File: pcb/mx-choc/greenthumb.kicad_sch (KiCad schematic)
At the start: 63 parts, among them J1 Conn_01x02_Female, M1 XIAO-RP2040, SW11 SW_Push, SW12 SW_Push, SW13 SW_Push, SW14 SW_Push, SW15 SW_Push, SW16 SW_Push, SW17 SW_Push, SW18 SW_Push, SW19 SW_Push, SW2 SW_Push, SW20 SW_Push, SW21 SW_Push, SW22 SW_Push, SW23 SW_Push, SW24 SW_Push, SW25 SW_Push, SW26 SW_Push, SW27 SW_Push, SW28 SW_Push, SW29 SW_Push, SW3 SW_Push, SW30 SW_Push, SW33 SW_Push, SW34 SW_Push, SW35 SW_Push, SW36 SW_Push, SW37 SW_Push, SW38 SW_Push, SW41 SW_Push, SW8 SW_Push, SW9 SW_Push

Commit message: routing almost done
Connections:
- net col0: now also SW35.2, SW36.2
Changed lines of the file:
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@@
   (junction (at 150.495 114.935) (diameter 0) (color 0 0 0 0)
+  )
+  (junction (at 133.985 114.935) (diameter 0) (color 0 0 0 0)
   )
   (junction (at 200.025 114.935) (diameter 0) (color 0 0 0 0)
@@
   )
   (junction (at 183.515 61.595) (diameter 0) (color 0 0 0 0)
+  )
+  (junction (at 133.985 88.265) (diameter 0) (color 0 0 0 0)
   )
   (junction (at 173.355 42.545) (diameter 0) (color 0 0 0 0)
@@
   )
   (wire (pts (xy 216.535 34.925) (xy 216.535 61.595))
+    (stroke (width 0) (type default) (color 0 0 0 0))
+  )
+  (wire (pts (xy 133.985 114.935) (xy 133.985 141.605))
     (stroke (width 0) (type default) (color 0 0 0 0))
   )
@@
     (stroke (width 0) (type default) (color 0 0 0 0))
   )
+  (wire (pts (xy 133.985 88.265) (xy 133.985 114.935))
+    (stroke (width 0) (type default) (color 0 0 0 0))
+  )

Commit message: completed pcb
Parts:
- added H1: MountingHole, fingerpunch:fingerpunch-logo, symbol Mechanical:MountingHole
- M1: LCSC (none) -> 102010428; Seeed SKU (none) -> 102010428
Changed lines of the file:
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@@
+      (effects (font (size 1.27 1.27)) hide)
+    )
+    (property "Seeed SKU" "" (id 5) (at 140.335 38.735 90)
       (effects (font (size 1.27 1.27)) hide)
     )
@@
       (effects (font (size 1.27 1.27)) hide)
     )
+    (property "Seeed SKU" "" (id 5) (at 156.845 38.735 90)
+      (effects (font (size 1.27 1.27)) hide)
+    )
     (pin "1")
     (pin "2")
@@
       (effects (font (size 1.27 1.27)) hide)
     )
+    (property "Seeed SKU" "" (id 5) (at 123.825 65.405 90)
+      (effects (font (size 1.27 1.27)) hide)
+    )
     (pin "1")
     (pin "2")
@@
       (effects (font (size 1.27 1.27)) hide)
     )
+    (property "Seeed SKU" "" (id 5) (at 140.335 65.405 90)
+      (effects (font (size 1.27 1.27)) hide)
+    )
     (pin "1")
     (pin "2")
@@
       (effects (font (size 1.27 1.27)) hide)
     )
+    (property "Seeed SKU" "" (id 5) (at 156.845 65.405 90)
+      (effects (font (size 1.27 1.27)) hide)
+    )
     (pin "1")
     (pin "2")
@@
       (effects (font (size 1.27 1.27)) hide)
     )
+    (property "Seeed SKU" "" (id 5) (at 173.355 65.405 90)
+      (effects (font (size 1.27 1.27)) hide)
+    )
     (pin "1")
     (pin "2")
@@
       (effects (font (size 1.27 1.27)) hide)
     )
+    (property "Seeed SKU" "" (id 5) (at 189.865 65.405 90)
+      (effects (font (size 1.27 1.27)) hide)
+    )
     (pin "1")
     (pin "2")
@@
       (effects (font (size 1.27 1.27)) hide)
     )
+    (property "Seeed SKU" "" (id 5) (at 206.375 65.405 90)
+      (effects (font (size 1.27 1.27)) hide)
+    )
     (pin "1")
     (pin "2")
@@
       (effects (font (size 1.27 1.27)) hide)
     )
+    (property "Seeed SKU" "" (id 5) (at 123.825 92.075 90)
+      (effects (font (size 1.27 1.27)) hide)
+    )
     (pin "1")
     (pin "2")
@@
       (effects (font (size 1.27 1.27)) hide)
     )
+    (property "Seeed SKU" "" (id 5) (at 140.335 92.075 90)
+      (effects (font (size 1.27 1.27)) hide)
+    )
     (pin "1")
     (pin "2")
@@
       (effects (font (size 1.27 1.27)) hide)
     )
+    (property "Seeed SKU" "" (id 5) (at 156.845 92.075 90)
+      (effects (font (size 1.27 1.27)) hide)
+    )
     (pin "1")
     (pin "2")
@@
       (effects (font (size 1.27 1.27)) hide)
     )
+    (property "Seeed SKU" "" (id 5) (at 173.355 92.075 90)
+      (effects (font (size 1.27 1.27)) hide)
+    )
     (pin "1")
     (pin "2")
@@
       (effects (font (size 1.27 1.27)) hide)
     )
+    (property "Seeed SKU" "" (id 5) (at 189.865 92.075 90)
+      (effects (font (size 1.27 1.27)) hide)
+    )
     (pin "1")
     (pin "2")
@@
       (effects (font (size 1.27 1.27)) hide)
     )
+    (property "Seeed SKU" "" (id 5) (at 206.375 92.075 90)
+      (effects (font (size 1.27 1.27)) hide)
+    )
     (pin "1")
     (pin "2")
@@
       (effects (font (size 1.27 1.27)) hide)
     )
+    (property "Seeed SKU" "" (id 5) (at 173.355 38.735 90)
+      (effects (font (size 1.27 1.27)) hide)
+    )
     (pin "1")
     (pin "2")
@@
       (effects (font (size 1.27 1.27)) hide)
     )
+    (property "Seeed SKU" "" (id 5) (at 189.865 38.735 90)
+      (effects (font (size 1.27 1.27)) hide)
+    )
     (pin "1")
     (pin "2")
@@
       (effects (font (size 1.27 1.27)) hide)
     )
+    (property "Seeed SKU" "" (id 5) (at 123.825 118.745 90)
+      (effects (font (size 1.27 1.27)) hide)
+    )
     (pin "1")
     (pin "2")
@@
       (effects (font (size 1.27 1.27)) hide)
     )
+    (property "Seeed SKU" "" (id 5) (at 123.825 145.415 90)
+      (effects (font (size 1.27 1.27)) hide)
+    )
     (pin "1")
     (pin "2")
@@
       (effects (font (size 1.27 1.27)) hide)
     )
+    (property "Seeed SKU" "" (id 5) (at 206.375 38.735 90)
+      (effects (font (size 1.27 1.27)) hide)
+    )
     (pin "1")
     (pin "2")
@@
       (effects (font (size 1.27 1.27)) hide)
     )
+    (property "Seeed SKU" "" (id 5) (at 206.375 145.415 90)
+      (effects (font (size 1.27 1.27)) hide)
+    )
     (pin "1")
     (pin "2")
@@
       (effects (font (size 1.27 1.27)) hide)
     )
+    (property "Seeed SKU" "" (id 5) (at 189.865 145.415 90)
+      (effects (font (size 1.27 1.27)) hide)
+    )
     (pin "1")
     (pin "2")
@@
       (effects (font (size 1.27 1.27)) hide)
     )
+    (property "Seeed SKU" "" (id 5) (at 156.845 145.415 90)
+      (effects (font (size 1.27 1.27)) hide)
+    )
     (pin "1")
     (pin "2")
@@
       (effects (font (size 1.27 1.27)) hide)
     )
+    (property "Seeed SKU" "" (id 5) (at 140.335 118.745 90)
+      (effects (font (size 1.27 1.27)) hide)
+    )
     (pin "1")
     (pin "2")
@@
       (effects (font (size 1.27 1.27)) hide)
     )
+    (property "Seeed SKU" "" (id 5) (at 140.335 145.415 90)
+      (effects (font (size 1.27 1.27)) hide)
+    )
     (pin "1")
     (pin "2")
@@
       (effects (font (size 1.27 1.27)) hide)
     )
+    (property "Seeed SKU" "" (id 5) (at 123.825 38.735 90)
+      (effects (font (size 1.27 1.27)) hide)
+    )
     (pin "1")
     (pin "2")
@@
       (effects (font (size 1.27 1.27)) hide)
     )
+    (property "Seeed SKU" "" (id 5) (at 173.355 118.745 90)
+      (effects (font (size 1.27 1.27)) hide)
+    )
     (pin "1")
     (pin "2")
@@
       (effects (font (size 1.27 1.27)) hide)
     )
+    (property "Seeed SKU" "" (id 5) (at 173.355 145.415 90)
+      (effects (font (size 1.27 1.27)) hide)
+    )
     (pin "1")
     (pin "2")
@@
       (effects (font (size 1.27 1.27)) hide)
     )
+    (property "Seeed SKU" "" (id 5) (at 156.845 118.745 90)
+      (effects (font (size 1.27 1.27)) hide)
+    )
     (pin "1")
     (pin "2")
@@
       (effects (font (size 1.27 1.27)) hide)
     )
+    (property "Seeed SKU" "" (id 5) (at 189.865 118.745 90)
+      (effects (font (size 1.27 1.27)) hide)
+    )
     (pin "1")
     (pin "2")
@@
       (effects (font (size 1.27 1.27)) hide)
     )
+    (property "Seeed SKU" "" (id 5) (at 206.375 118.745 90)
+      (effects (font (size 1.27 1.27)) hide)
+    )
     (pin "1")
     (pin "2")
@@
     )
     (property "Datasheet" "~" (id 3) (at 39.37 103.505 0)
+      (effects (font (size 1.27 1.27)) hide)
+    )
+    (property "Seeed SKU" "" (id 4) (at 39.37 108.585 0)
       (effects (font (size 1.27 1.27)) hide)
     )
@@
     )
     (property "Datasheet" "" (id 3) (at 40.64 58.42 0)
+      (effects (font (size 1.27 1.27)) hide)
+    )
+    (property "LCSC" "102010428" (id 4) (at 40.64 58.42 0)
+      (effects (font (size 1.27 1.27)) hide)
+    )
+    (property "Seeed SKU" "102010428" (id 5) (at 40.64 58.42 0)
       (effects (font (size 1.27 1.27)) hide)
     )
@@
     (pin "9")
   )
+  (symbol (lib_id "Mechanical:MountingHole") (at 48.26 151.13 0) (unit 1)
+    (in_bom yes) (on_board yes) (fields_autoplaced)
+    (property "Reference" "H1" (id 0) (at 50.8 149.8599 0)
+      (effects (font (size 1.27 1.27)) (justify left))
+    )
+    (property "Value" "MountingHole" (id 1) (at 50.8 152.3999 0)
+      (effects (font (size 1.27 1.27)) (justify left))
+    )
+    (property "Footprint" "fingerpunch:fingerpunch-logo" (id 2) (at 48.26 151.13 0)
+      (effects (font (size 1.27 1.27)) hide)
+    )
+    (property "Datasheet" "~" (id 3) (at 48.26 151.13 0)
+      (effects (font (size 1.27 1.27)) hide)
+    )
+  )
   (symbol (lib_id "power:+5V") (at 60.96 50.8 270) (unit 1)
     (in_bom yes) (on_board yes)
@@
       (reference "D38") (unit 1) (value "1N4148W") (footprint "Diode_SMD:D_SOD-123")
     )
+    (path "/ae2e9f51-3260-4b87-b717-00da647401fb"
+      (reference "H1") (unit 1) (value "MountingHole") (footprint "fingerpunch:fingerpunch-logo")
+    )
     (path "/60a97046-6b57-40f0-b47f-57b153d7286d"

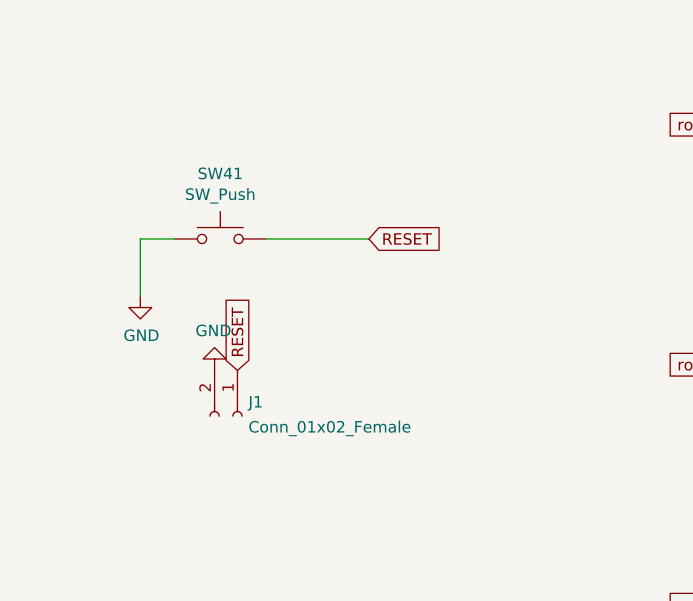
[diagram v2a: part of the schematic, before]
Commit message: removed reset switch, as it wasn't being used, and no way to hook it up to the seeeduino
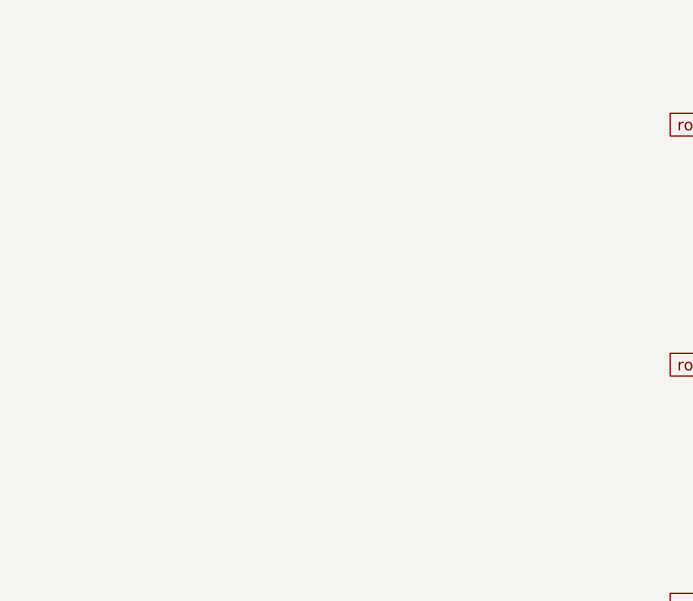
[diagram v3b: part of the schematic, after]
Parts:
- removed J1: Conn_01x02_Female, fingerpunch:Connector_THT_1x2_2.54, symbol Connector:Conn_01x02_Female
- removed SW41: SW_Push, random-keyboard-parts:SKQG-1155865, symbol Switch:SW_Push
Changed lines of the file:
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@@
-    (stroke (width 0) (type default) (color 0 0 0 0))
-  )
-  (wire (pts (xy 44.45 108.585) (xy 55.88 108.585))
     (stroke (width 0) (type default) (color 0 0 0 0))
   )
@@
     (stroke (width 0) (type default) (color 0 0 0 0))
   )
-  (wire (pts (xy 30.48 108.585) (xy 30.48 114.935))
-    (stroke (width 0) (type default) (color 0 0 0 0))
-  )
   (wire (pts (xy 63.5 24.13) (xy 63.5 26.67))
     (stroke (width 0) (type default) (color 0 0 0 0))
@@
   )
   (wire (pts (xy 140.335 122.555) (xy 156.845 122.555))
-    (stroke (width 0) (type default) (color 0 0 0 0))
-  )
-  (wire (pts (xy 30.48 108.585) (xy 34.29 108.585))
     (stroke (width 0) (type default) (color 0 0 0 0))
   )
@@
     )
   )
-  (global_label "RESET" (shape input) (at 55.88 108.585 0) (fields_autoplaced)
-    (effects (font (size 1.27 1.27)) (justify left))
-    (property "Intersheet References" "${INTERSHEET_REFS}" (id 0) (at -11.43 -102.235 0)
-      (effects (font (size 1.27 1.27)) hide)
-    )
-  )
-  (global_label "RESET" (shape input) (at 41.275 123.19 90) (fields_autoplaced)
-    (effects (font (size 1.27 1.27)) (justify left))
-    (property "Intersheet References" "${INTERSHEET_REFS}" (id 0) (at -169.545 190.5 0)
-      (effects (font (size 1.27 1.27)) hide)
-    )
-  )
   (global_label "row4" (shape input) (at 57.15 58.42 0) (fields_autoplaced)
     (effects (font (size 1.27 1.27)) (justify left))
@@
     )
   )
-  (symbol (lib_id "power:GND") (at 30.48 114.935 0) (unit 1)
-    (in_bom yes) (on_board yes)
-    (property "Reference" "#PWR013" (id 0) (at 30.48 121.285 0)
-      (effects (font (size 1.27 1.27)) hide)
-    )
-    (property "Value" "GND" (id 1) (at 30.607 119.3292 0))
-    (property "Footprint" "" (id 2) (at 30.48 114.935 0)
-      (effects (font (size 1.27 1.27)) hide)
-    )
-    (property "Datasheet" "" (id 3) (at 30.48 114.935 0)
-      (effects (font (size 1.27 1.27)) hide)
-    )
-    (pin "1")
-  )
   (symbol (lib_id "Switch:SW_Push") (at 145.415 34.925 0) (unit 1)
     (in_bom yes) (on_board yes)
@@
     (pin "2")
   )
-  (symbol (lib_id "Switch:SW_Push") (at 39.37 108.585 0) (unit 1)
-    (in_bom yes) (on_board yes)
-    (property "Reference" "SW41" (id 0) (at 39.37 101.346 0))
-    (property "Value" "SW_Push" (id 1) (at 39.37 103.6574 0))
-    (property "Footprint" "random-keyboard-parts:SKQG-1155865" (id 2) (at 39.37 103.505 0)
-      (effects (font (size 1.27 1.27)) hide)
-    )
-    (property "Datasheet" "~" (id 3) (at 39.37 103.505 0)
-      (effects (font (size 1.27 1.27)) hide)
-    )
-    (property "Seeed SKU" "" (id 4) (at 39.37 108.585 0)
-      (effects (font (size 1.27 1.27)) hide)
-    )
-    (pin "1")
-    (pin "2")
-  )
   (symbol (lib_id "power:GND") (at 60.96 53.34 90) (unit 1)
     (in_bom yes) (on_board yes)
@@
     )
     (pin "1")
-  )
-  (symbol (lib_id "Connector:Conn_01x02_Female") (at 41.275 128.27 270) (unit 1)
-    (in_bom yes) (on_board yes) (fields_autoplaced)
-    (property "Reference" "J1" (id 0) (at 42.4942 126.7265 90)
-      (effects (font (size 1.27 1.27)) (justify left))
-    )
-    (property "Value" "Conn_01x02_Female" (id 1) (at 42.4942 129.5016 90)
-      (effects (font (size 1.27 1.27)) (justify left))
-    )
-    (property "Footprint" "fingerpunch:Connector_THT_1x2_2.54" (id 2) (at 41.275 128.27 0)
-      (effects (font (size 1.27 1.27)) hide)
-    )
-    (property "Datasheet" "~" (id 3) (at 41.275 128.27 0)
-      (effects (font (size 1.27 1.27)) hide)
-    )
-    (pin "1")
-    (pin "2")
   )
   (symbol (lib_id "xiao-rp2040:XIAO-RP2040") (at 40.64 58.42 0) (unit 1)
@@
     (pin "1")
   )
-  (symbol (lib_id "power:GND") (at 38.735 123.19 180) (unit 1)
-    (in_bom yes) (on_board yes)
-    (property "Reference" "#PWR0102" (id 0) (at 38.735 116.84 0)
-      (effects (font (size 1.27 1.27)) hide)
-    )
-    (property "Value" "GND" (id 1) (at 38.608 118.7958 0))
-    (property "Footprint" "" (id 2) (at 38.735 123.19 0)
-      (effects (font (size 1.27 1.27)) hide)
-    )
-    (property "Datasheet" "" (id 3) (at 38.735 123.19 0)
-      (effects (font (size 1.27 1.27)) hide)
-    )
-    (pin "1")
-  )
   (sheet_instances
     (path "/" (page "1"))
@@
       (reference "#FLG0103") (unit 1) (value "PWR_FLAG") (footprint "")
     )
-    (path "/00000000-0000-0000-0000-000060e827d4"
-      (reference "#PWR013") (unit 1) (value "GND") (footprint "")
-    )
     (path "/b29b27e5-2828-4838-8d1f-985db095879f"
       (reference "#PWR0101") (unit 1) (value "+5V") (footprint "")
     )
-    (path "/cb353616-17b0-4aff-a99b-5f9946e06454"
-      (reference "#PWR0102") (unit 1) (value "GND") (footprint "")
-    )
     (path "/00000000-0000-0000-0000-000060f9d11d"
       (reference "#PWR0103") (unit 1) (value "VCC") (footprint "")
@@
       (reference "H1") (unit 1) (value "MountingHole") (footprint "fingerpunch:fingerpunch-logo")
     )
-    (path "/60a97046-6b57-40f0-b47f-57b153d7286d"
-      (reference "J1") (unit 1) (value "Conn_01x02_Female") (footprint "fingerpunch:Connector_THT_1x2_2.54")
-    )
     (path "/6e45ce63-3616-442c-b187-999f887ac89b"
       (reference "M1") (unit 1) (value "XIAO-RP2040") (footprint "fingerpunch:XIAO-RP2040")
@@
       (reference "SW38") (unit 1) (value "SW_Push") (footprint "fingerpunch:Kailh_socket_MX-ChocV1")
     )
-    (path "/00000000-0000-0000-0000-0000613137a2"
-      (reference "SW41") (unit 1) (value "SW_Push") (footprint "random-keyboard-parts:SKQG-1155865")
-    )
-  )
+  )
